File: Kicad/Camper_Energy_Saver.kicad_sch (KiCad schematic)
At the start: 68 parts, among them J1 IDC_13X2, J10 Conn_01x01_Pin, J11 Conn_01x01_Pin, J2 Conn_01x03_Pin, J3 Conn_01x03_Pin, J4 IDC_5X2, J5 Conn_01x03_Pin, J6 Conn_01x01_Pin, J7 Conn_01x01_Pin, J8 Conn_01x01_Pin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

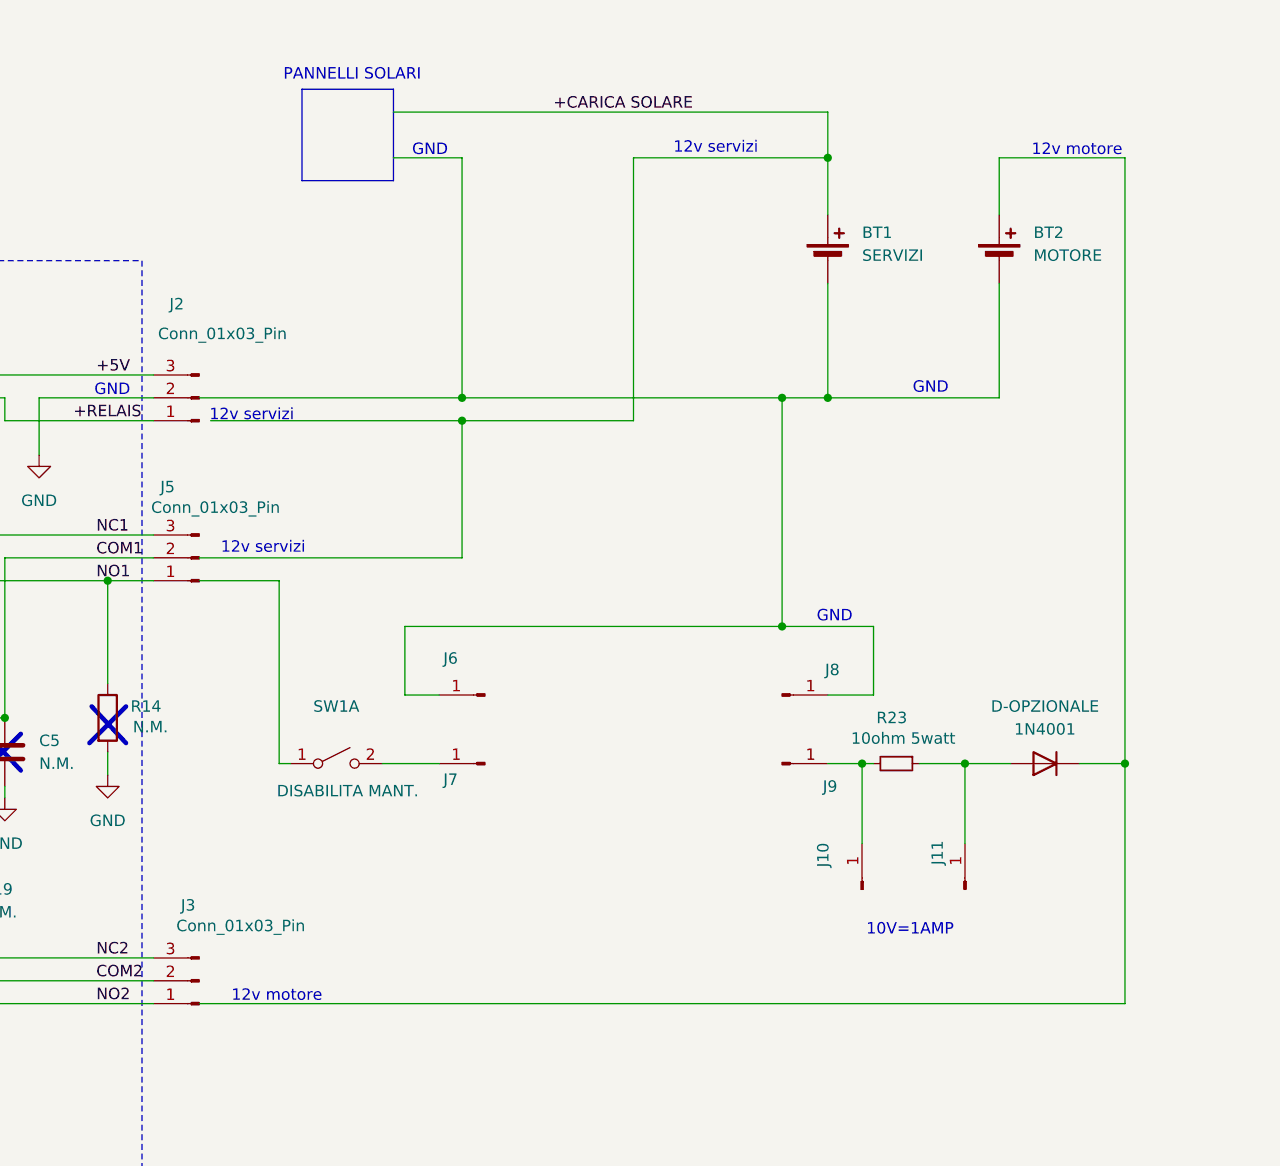
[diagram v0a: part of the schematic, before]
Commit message: aggiinto rele di potenza
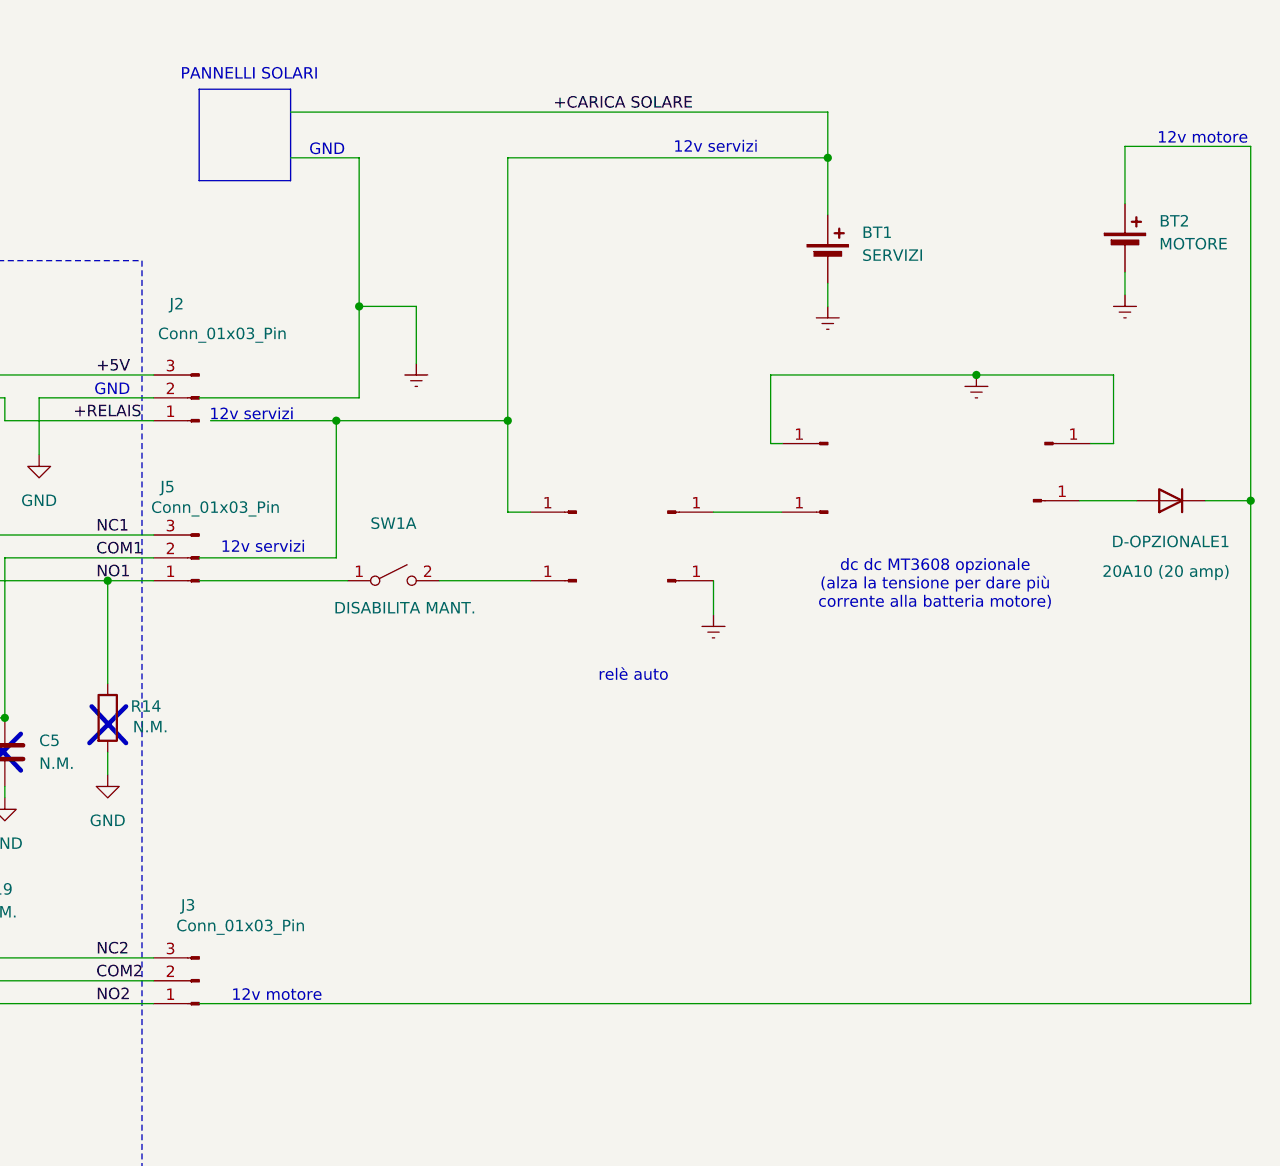
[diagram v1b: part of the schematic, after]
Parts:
- removed D-OPZIONALE: 1N4001, Diode_THT:D_DO-41_SOD81_P10.16mm_Horizontal, symbol Diode:1N4001
- removed R23: 10ohm 5watt, Resistor_THT:R_Axial_DIN0204_L3.6mm_D1.6mm_P2.54mm_Vertical, symbol Device:R_Small
- added D-OPZIONALE1: 20A10 (20 amp), Diode_THT:D_DO-41_SOD81_P10.16mm_Horizontal, symbol Diode:1N4001
- added J12, J13: Conn_01x01_Pin, symbol Connector:Conn_01x01_Pin
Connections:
- net +CARICA SOLARE: now also J11.1 (Pin_1)
- net at SW1.2 (B): now also J10.1 (Pin_1); no longer J7.1 (Pin_1)
- net at BT2.1 (+): now also D-OPZIONALE1.1 (K)
- net GNDREF: now reaches BT1.2 (-), BT2.2 (-), J6.1 (Pin_1), J8.1 (Pin_1)
- net GNDREF: now also J12.1 (Pin_1)
- net at J9.1 (Pin_1): now also D-OPZIONALE1.2 (A); no longer J10.1 (Pin_1)
- new net: J13.1 (Pin_1), J7.1 (Pin_1)
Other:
- note added: "dc dc MT3608 opzionale (alza la tensione per dare più corrente alla batteria motore)"
- note added: "relè auto"
- note removed: "10V=1AMP"
- moved on the sheet: BT2, SW1A

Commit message: aggiornamento
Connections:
- net +CARICA SOLARE: no longer J11.1 (Pin_1)
- net GNDREF: no longer BT1.2 (-), BT2.2 (-)
- net at BT2.1 (+): no longer D-OPZIONALE1.1 (K)
- new net: BT1.2 (-), BT2.2 (-)
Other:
- title: Amperometro con soglia -> PARALLELATORE BATTERIE CAMPER
- moved on the sheet: A1, BT1, BT2, BZ1, C1, C2, C3, C4, C5, C6, D-OPZIONALE1, D1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
